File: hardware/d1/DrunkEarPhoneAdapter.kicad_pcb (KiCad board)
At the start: 2 copper layers, 40.3 x 34.7 mm, 9 parts, among them U1 CS43131-CNZR, U2 STM32G0B1VCT6, U4 TCPP03-M20, U5 TCPP03-M20, U6 ES8327, X1 X322516MLB4SI, X2 OT7EL89CJI-111YLC-24_576M

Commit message: New components
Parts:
- added R1: 10k, Resistor_SMD:R_0603_1608Metric, F.Cu at (28.3, 24.2)
- added U7: TPS7A2018PDBVR, JLCImport:TPS7A2018PDBVR, F.Cu at (30.1, 30.8)
- added U8: TPS7A2033PDBVR, JLCImport:TPS7A2033PDBVR, F.Cu at (24.9, 26.5)
- added U9: TPS560430XFDBVR, JLCImport:TPS560430XFDBVR, F.Cu at (25.2, 30.8)
- moved U6 17.5 mm to (44.3, 48.3)
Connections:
- U1 pad 38: unconnected-(U1-LRCK1-Pad38) -> /dac/I2S_WS
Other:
- copper layers 2 -> 4

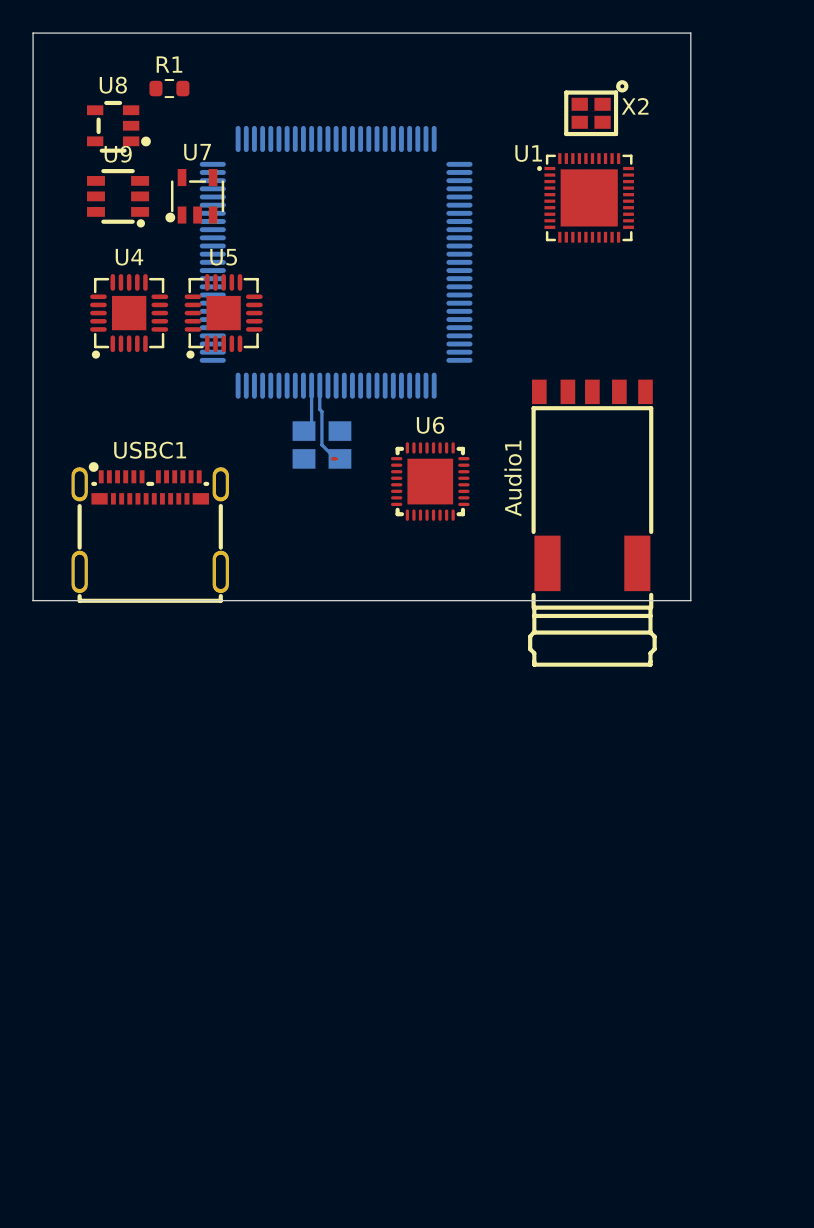
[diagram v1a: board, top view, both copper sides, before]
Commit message: Change uart pins, add components
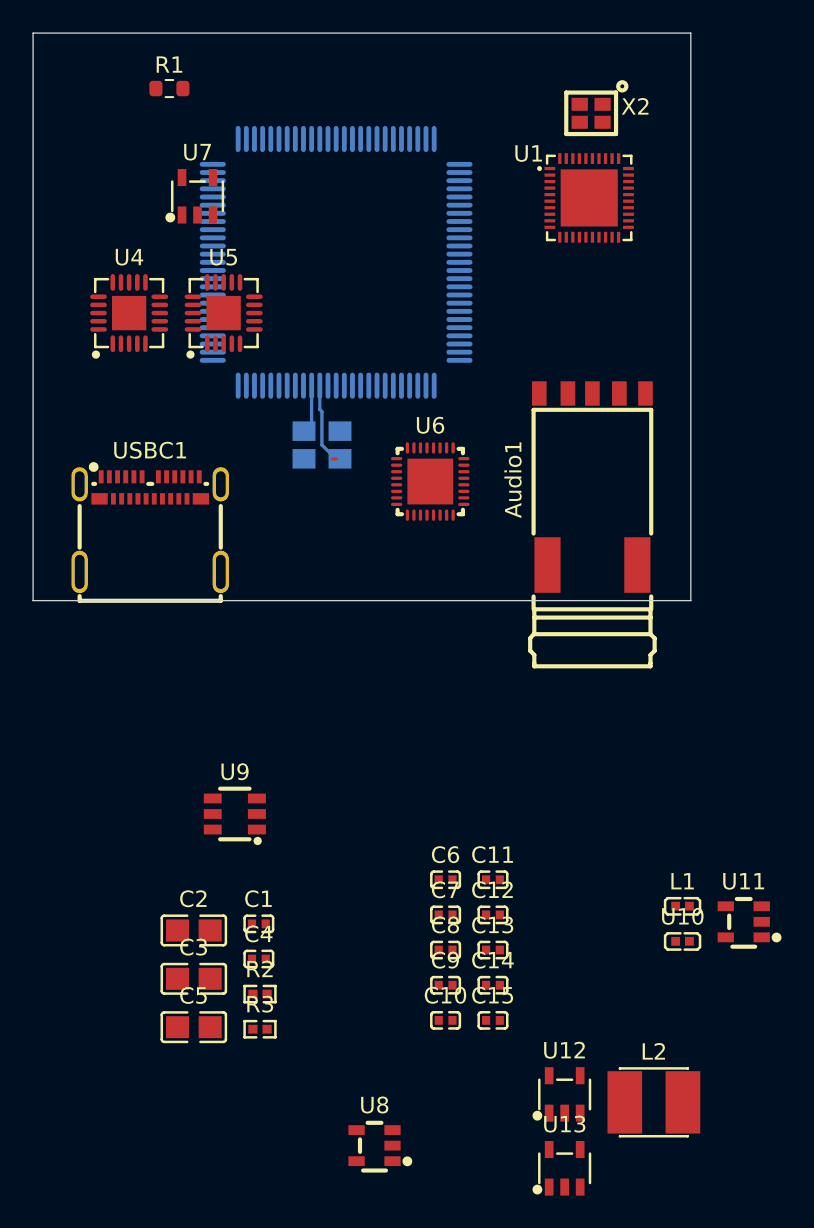
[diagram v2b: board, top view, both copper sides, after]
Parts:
- added C1: 100nF 16V X7R, JLCImport:CL05B104KO5NNNC, F.Cu at (33.8, 75.4)
- added C10: 1uF 25V X5R, JLCImport:CL05A105KA5NQNC, F.Cu at (45.2, 81.3)
- added C11: 1uF 25V X5R, JLCImport:CL05A105KA5NQNC, F.Cu at (48.1, 72.7)
- added C12: 1uF 25V X5R, JLCImport:CL05A105KA5NQNC, F.Cu at (48.1, 74.8)
- added C13: 4.7uF 10V X5R, JLCImport:CL05A475MP5NRNC, F.Cu at (48.1, 77.0)
- added C14: 1uF 25V X5R, JLCImport:CL05A105KA5NQNC, F.Cu at (48.1, 79.1)
- added C15: 1uF 25V X5R, JLCImport:CL05A105KA5NQNC, F.Cu at (48.1, 81.3)
- added C2: 2.2uF 50V X7R, JLCImport:CC0805KKX7R9BB225, F.Cu at (29.8, 75.8)
- added C3: 2.2uF 50V X7R, JLCImport:CC0805KKX7R9BB225, F.Cu at (29.8, 78.7)
- added C4: 100nF 50V X7R, JLCImport:CL05B104KB54PNC, F.Cu at (33.8, 77.5)
- added C5: 22uF 25V X5R, JLCImport:CL21A226MAQNNNE, F.Cu at (29.8, 81.7)
- added C6: 1uF 25V X5R, JLCImport:CL05A105KA5NQNC, F.Cu at (45.2, 72.7)
- added C7: 4.7uF 10V X5R, JLCImport:CL05A475MP5NRNC, F.Cu at (45.2, 74.8)
- added C8: 1uF 25V X5R, JLCImport:CL05A105KA5NQNC, F.Cu at (45.2, 77.0)
- added C9: 1uF 25V X5R, JLCImport:CL05A105KA5NQNC, F.Cu at (45.2, 79.1)
- added L1: BLM15AG601SN1D, JLCImport:BLM15AG601SN1D, F.Cu at (59.8, 74.3)
- added L2: SWPA4020S150MT, JLCImport:SWPA4020S150MT, F.Cu at (58.0, 86.3)
- added R2: 62kΩ, JLCImport:0402WGF6202TCE, F.Cu at (33.9, 79.7)
- added R3: 22kΩ, JLCImport:0402WGF2202TCE, F.Cu at (33.9, 81.8)
- added U10: BLM15PX601SN1D, JLCImport:BLM15PX601SN1D, F.Cu at (59.8, 76.4)
- added U11: TPS7A2033PDBVR, JLCImport:TPS7A2033PDBVR, F.Cu at (63.5, 75.3)
- added U12: TPS7A2018PDBVR, JLCImport:TPS7A2018PDBVR, F.Cu at (52.5, 85.8)
- added U13: TPS7A2018PDBVR, JLCImport:TPS7A2018PDBVR, F.Cu at (52.5, 90.3)
- moved U8 64.4 mm to (40.9, 89.0)
- moved U9 38.5 mm to (32.4, 68.7)
- moved Audio1 0.10 mm to (54.2, 48.2)
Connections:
- net /dac/JACK_RING_2 renamed /headset/JACK_RING_2
- Audio1 pad 1: /dac/JACK_SLEEVE -> /headset/JACK_SLEEVE
- Audio1 pad 2: /dac/JACK_TIP_DETECT -> /headset/JACK_TIP_DETECT
- Audio1 pad 3: /dac/JACK_RING_1 -> /headset/JACK_RING_1
- Audio1 pad 5: /dac/JACK_TIP -> /headset/JACK_TIP
- U7 pad 1: unconnected-(U7-IN-Pad1) -> +3V8
- U7 pad 2: unconnected-(U7-GND-Pad2) -> GND
- U7 pad 3: unconnected-(U7-EN-Pad3) -> +3V8
- U7 pad 5: unconnected-(U7-OUT-Pad5) -> +1V8_D
- U8 pad 3: unconnected-(U8-EN-Pad3) -> +1V8_D
- U8 pad 5: unconnected-(U8-OUT-Pad5) -> +3V3_D
- U9 pad 1: unconnected-(U9-CB-Pad1) -> Net-(U9-CB)
- U9 pad 2: unconnected-(U9-GND-Pad2) -> GND
- U9 pad 3: unconnected-(U9-FB-Pad3) -> Net-(U9-FB)
- U9 pad 4: unconnected-(U9-EN-Pad4) -> PWR_IN
- U9 pad 5: unconnected-(U9-VIN-Pad5) -> PWR_IN
- U9 pad 6: unconnected-(U9-SW-Pad6) -> Net-(U9-SW)

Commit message: Add new parts
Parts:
- removed R1: 10k, Resistor_SMD:R_0603_1608Metric
- added C16: 4.7uF 10V X5R, JLCImport:CL05A475MP5NRNC, F.Cu at (27.4, 104.2)
- added C17: 1uF 25V X5R, JLCImport:CL05A105KA5NQNC, F.Cu at (27.4, 106.3)
- added C18: 1uF 25V X5R, JLCImport:CL05A105KA5NQNC, F.Cu at (35.6, 104.2)
- added C19: 100nF 16V X7R, JLCImport:CL05B104KO5NNNC, F.Cu at (27.4, 108.5)
- added C20: 100nF 16V X7R, JLCImport:CL05B104KO5NNNC, F.Cu at (35.6, 106.3)
- added C21: 100nF 16V X7R, JLCImport:CL05B104KO5NNNC, F.Cu at (27.4, 110.6)
- added C22: 100nF 16V X7R, JLCImport:CL05B104KO5NNNC, F.Cu at (27.4, 112.8)
- added C23: 100nF 16V X7R, JLCImport:CL05B104KO5NNNC, F.Cu at (27.4, 114.9)
- added C24: 100nF 16V X7R, JLCImport:CL05B104KO5NNNC, F.Cu at (55.2, 101.9)
- added C25: 2.2uF 16V X5R, JLCImport:CL05A225KO5NQNC, F.Cu at (55.2, 104.0)
- added C26: 15uF 35V X5R, JLCImport:C2012X5R1V156MT000E, F.Cu at (59.2, 102.3)
- added C27: 15uF 35V X5R, JLCImport:C2012X5R1V156MT000E, F.Cu at (59.2, 105.2)
- added C28: 2.2uF 16V X5R, JLCImport:CL05A225KO5NQNC, F.Cu at (55.2, 106.2)
- added C29: 2.2uF 16V X5R, JLCImport:CL05A225KO5NQNC, F.Cu at (51.4, 117.7)
- added C30: 2.2uF 16V X5R, JLCImport:CL05A225KO5NQNC, F.Cu at (51.4, 119.8)
- added C31: 2.2uF 16V X5R, JLCImport:CL05A225KO5NQNC, F.Cu at (51.4, 122.0)
- added C32: 2.2uF 16V X5R, JLCImport:CL05A225KO5NQNC, F.Cu at (51.4, 124.1)
- added C33: 2.2uF 16V X5R, JLCImport:CL05A225KO5NQNC, F.Cu at (51.4, 126.3)
- added C34: 2.2uF 16V X5R, JLCImport:CL05A225KO5NQNC, F.Cu at (51.4, 128.4)
- added L3: BLM15AG601SN1D, JLCImport:BLM15AG601SN1D, F.Cu at (30.5, 106.3)
- added L4: BLM15AG601SN1D, JLCImport:BLM15AG601SN1D, F.Cu at (38.7, 104.2)
- added U14: BLM15PX601SN1D, JLCImport:BLM15PX601SN1D, F.Cu at (30.5, 108.5)
- moved L1 37.0 mm to (30.4, 96.9)
- moved X2 0.60 mm to (53.9, 26.3)
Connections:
- net /dac/JACK_SLEEVE renamed /dac/JACK_DETECTED_GND
- C12 pad 2: +3V8 -> Net-(U12-EN)
- L1 pad 1: unconnected-(L1-Pad1) -> +1V8_D
- L1 pad 2: unconnected-(L1-Pad2) -> Net-(X2-VDD)
- U1 pad 10: unconnected-(U1-FLYP_VA-Pad10) -> /dac/FLYP_VA
- U1 pad 11: unconnected-(U1-FLYN_VA-Pad11) -> /dac/FLYN_VA
- U1 pad 18: unconnected-(U1-VCP_FILT–-Pad18) -> /dac/VCP_FILT-
- U1 pad 19: unconnected-(U1-GNDCP-Pad19) -> /dac/GNDCP
- U1 pad 20: unconnected-(U1-FLYN_VCP-Pad20) -> /dac/FLYN_VCP
- U1 pad 21: unconnected-(U1-VCP_FILT+-Pad21) -> /dac/VCP_FILT+
- U1 pad 23: unconnected-(U1-FLYC_VCP-Pad23) -> /dac/FLYC_VCP
- U1 pad 24: unconnected-(U1-FLYP_VCP-Pad24) -> /dac/FLYP_VCP
- U1 pad 25: unconnected-(U1-VCP-Pad25) -> /dac/VCP
- U1 pad 26: unconnected-(U1-VP-Pad26) -> Net-(U1-VP)
- U1 pad 28: unconnected-(U1-RESET#-Pad28) -> /dac/DAC_RESET
- U1 pad 31: unconnected-(U1-VL-Pad31) -> Net-(U1-VD)
- U1 pad 35: unconnected-(U1-GNDD-Pad35) -> GND
- U1 pad 4: unconnected-(U1-VD-Pad4) -> Net-(U1-VD)
- U1 pad 41: unconnected-(U1-EP-Pad41) -> GND
- U1 pad 5: unconnected-(U1-FILT+-Pad5) -> /dac/FILT+
- U1 pad 6: unconnected-(U1-FILT–-Pad6) -> /dac/FILT-
- U1 pad 7: unconnected-(U1-VA-Pad7) -> +1V8_A
- U1 pad 8: unconnected-(U1-GNDA-Pad8) -> GND
- U1 pad 9: unconnected-(U1--VA-Pad9) -> /dac/-VA
- U10 pad 1: unconnected-(U10-Pad1) -> +3V8
- U10 pad 2: unconnected-(U10-Pad2) -> Net-(U12-EN)
- U12 pad 1: +3V8 -> Net-(U12-EN)
- U12 pad 3: +3V8 -> Net-(U12-EN)
- U2 pad 12: unconnected-(U2-VREF+-Pad12) -> Net-(U2-VREF+)
- U2 pad 14: unconnected-(U2-VSS/VSSA-Pad14) -> GND
- U2 pad 19: /mcu/UART_TX -> unconnected-(U2-PF4-Pad19)
- U2 pad 20: /mcu/UART_RX -> unconnected-(U2-PF5-Pad20)
- U2 pad 57: unconnected-(U2-PC6-Pad57) -> /mcu/UART_TX
- U2 pad 58: unconnected-(U2-PC7-Pad58) -> /mcu/UART_RX
- U2 pad 63: unconnected-(U2-VSS-Pad63) -> GND
- X1 pad 2: GND -> Net-(X1-GND-Pad2)
- X1 pad 4: GND -> Net-(X1-GND-Pad2)
- X2 pad 2: unconnected-(X2-GND-Pad2) -> GND
- X2 pad 4: unconnected-(X2-VDD-Pad4) -> Net-(X2-VDD)
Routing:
- net Net-(U1-XTI/MCLK): track 0.00 -> 1.78 mm

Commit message: Pre-finalize sch
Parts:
- removed X2: OT7EL89CJI-111YLC-24_576M, JLCImport:OT7EL89CJI-111YLC-24_576M
- added C35: 100nF 16V X7R, JLCImport:CL05B104KO5NNNC, F.Cu at (78.8, 71.6)
- added C36: 1uF 25V X5R, JLCImport:CL05A105KA5NQNC, F.Cu at (78.8, 73.7)
- added C37: 100nF 16V X7R, JLCImport:CL05B104KO5NNNC, F.Cu at (78.8, 75.9)
- added C38: 1uF 25V X5R, JLCImport:CL05A105KA5NQNC, F.Cu at (81.7, 71.6)
- added C39: 100nF 16V X7R, JLCImport:CL05B104KO5NNNC, F.Cu at (81.7, 73.7)
- added C40: 100nF 16V X7R, JLCImport:CL05B104KO5NNNC, F.Cu at (81.7, 75.9)
- added C41: 1uF 25V X5R, JLCImport:CL05A105KA5NQNC, F.Cu at (84.6, 71.6)
- added C42: 1uF 25V X5R, JLCImport:CL05A105KA5NQNC, F.Cu at (84.6, 73.7)
- added C43: 1uF 25V X5R, JLCImport:CL05A105KA5NQNC, F.Cu at (84.6, 75.9)
- added C44: 100nF 16V X7R, JLCImport:CL05B104KO5NNNC, F.Cu at (96.6, 61.8)
- added C45: 1uF 25V X5R, JLCImport:CL05A105KA5NQNC, F.Cu at (88.8, 51.9)
- added C46: 1uF 25V X5R, JLCImport:CL05A105KA5NQNC, F.Cu at (88.8, 54.0)
- added C47: 1uF 25V X5R, JLCImport:CL05A105KA5NQNC, F.Cu at (88.8, 56.2)
- added C48: 1uF 25V X5R, JLCImport:CL05A105KA5NQNC, F.Cu at (88.8, 58.3)
- added C49: 10nF 50V X7R, Capacitor_SMD:C_0402_1005Metric, F.Cu at (41.4, 125.2)
- added C50: 100nF 16V X7R, JLCImport:CL05B104KO5NNNC, F.Cu at (38.5, 121.0)
- added C51: 22uF 25V X5R, JLCImport:CL21A226MAQNNNE, F.Cu at (86.4, 30.9)
- added C52: 100nF 16V X7R, JLCImport:CL05B104KO5NNNC, F.Cu at (38.5, 123.1)
- added C53: 4.7uF 10V X5R, JLCImport:CL05A475MP5NRNC, F.Cu at (38.5, 125.3)
- added C54: 100nF 16V X7R, JLCImport:CL05B104KO5NNNC, F.Cu at (38.5, 127.4)
- added C55: 4.7uF 10V X5R, JLCImport:CL05A475MP5NRNC, F.Cu at (38.5, 129.6)
- added C56: 100nF 16V X7R, JLCImport:CL05B104KO5NNNC, F.Cu at (96.8, 43.9)
- added C57: 22uF 25V X5R, JLCImport:CL21A226MAQNNNE, F.Cu at (86.4, 33.8)
- added C58: 22uF 25V X5R, JLCImport:CL21A226MAQNNNE, F.Cu at (86.4, 36.8)
- added C59: 22uF 25V X5R, JLCImport:CL21A226MAQNNNE, F.Cu at (86.4, 39.8)
- added C60: 22uF 25V X5R, JLCImport:CL21A226MAQNNNE, F.Cu at (86.4, 42.7)
- added C61: 22uF 25V X5R, JLCImport:CL21A226MAQNNNE, F.Cu at (86.4, 45.7)
- added C62: 22uF 25V X5R, JLCImport:CL21A226MAQNNNE, F.Cu at (86.4, 48.6)
- added C63: 22uF 25V X5R, JLCImport:CL21A226MAQNNNE, F.Cu at (86.4, 51.6)
- added C64: 22uF 25V X5R, JLCImport:CL21A226MAQNNNE, F.Cu at (86.4, 54.6)
- added C65: 22uF 25V X5R, JLCImport:CL21A226MAQNNNE, F.Cu at (86.4, 57.5)
- added C66: 10nF 50V X7R, Capacitor_SMD:C_0402_1005Metric, F.Cu at (8.91, 17.3)
- added C67: 2.2uF 50V X7R, JLCImport:CC0805KKX7R9BB225, F.Cu at (4.95, 15.6)
- added C68: 2.2uF 50V X7R, JLCImport:CC0805KKX7R9BB225, F.Cu at (4.95, 18.6)
- added C69: 100nF 50V X7R, JLCImport:CL05B104KB54PNC, F.Cu at (8.93, 15.2)
- added C70: 330pF 50V, Capacitor_SMD:C_0402_1005Metric, F.Cu at (93.1, 88.3)
- added C71: 330pF 50V, Capacitor_SMD:C_0402_1005Metric, F.Cu at (93.1, 90.3)
- added C72: 330pF 50V, Capacitor_SMD:C_0402_1005Metric, F.Cu at (93.1, 92.2)
- added C73: 330pF 50V, Capacitor_SMD:C_0402_1005Metric, F.Cu at (93.1, 94.2)
- added C74: 100nF 16V X7R, JLCImport:CL05B104KO5NNNC, F.Cu at (78.6, 102.4)
- added C75: 100nF 50V X7R, JLCImport:CL05B104KB54PNC, F.Cu at (78.6, 104.5)
- added C76: 1uF 25V X5R, JLCImport:CL05A105KA5NQNC, F.Cu at (83.4, 106.7)
- added C77: 100nF 16V X7R, JLCImport:CL05B104KO5NNNC, F.Cu at (83.4, 108.8)
- added C78: 100nF 16V X7R, JLCImport:CL05B104KO5NNNC, F.Cu at (83.4, 111.0)
- added C79: 100nF 16V X7R, JLCImport:CL05B104KO5NNNC, F.Cu at (83.4, 113.1)
- added D1: PMEG4010CEH_115, Diode_SMD:D_SOD-110, F.Cu at (97.5, 36.3)
- added D2: B5819WS_C916992, Diode_SMD:D_SOD-323, F.Cu at (91.1, 33.8)
- added D3: PMEG4010CEH_115, Diode_SMD:D_SOD-110, F.Cu at (97.5, 39.3)
- added L5: BLM15AG601SN1D, JLCImport:BLM15AG601SN1D, F.Cu at (79.0, 78.0)
- added L6: BLM15AG601SN1D, JLCImport:BLM15AG601SN1D, F.Cu at (79.0, 80.2)
- added L7: ECMF02-2AMX6, JLCImport:ECMF02-2AMX6, F.Cu at (103.5, 88.2)
- added Q1: CSD17577Q3A, JLCImport:CSD17577Q3A, F.Cu at (24.1, 30.5)
- added Q2: CSD17577Q3A, JLCImport:CSD17577Q3A, F.Cu at (24.0, 23.9)
- added R1: 33Ω, Resistor_SMD:R_0402_1005Metric, F.Cu at (96.1, 102.3)
- added R10: 10kΩ, Resistor_SMD:R_0402_1005Metric, F.Cu at (91.7, 51.8)
- added R11: 2.2kΩ, Resistor_SMD:R_0402_1005Metric, F.Cu at (96.7, 51.8)
- added R12: 2.2kΩ, Resistor_SMD:R_0402_1005Metric, F.Cu at (96.7, 53.8)
- added R13: 10kΩ, Resistor_SMD:R_0402_1005Metric, F.Cu at (91.7, 53.8)
- added R14: 100kΩ, JLCImport:0402WGF1003TCE, F.Cu at (41.5, 121.0)
- added R15: 100kΩ, JLCImport:0402WGF1003TCE, F.Cu at (41.5, 123.1)
- added R16: 33Ω 0805, Resistor_SMD:R_0805_2012Metric, F.Cu at (91.2, 30.9)
- added R17: 10mΩ 500mW, Resistor_SMD:R_0805_2012Metric, F.Cu at (101.9, 36.2)
- added R18: 10mΩ 500mW, Resistor_SMD:R_0805_2012Metric, F.Cu at (101.9, 39.2)
- added R19: 10kΩ, Resistor_SMD:R_0402_1005Metric, F.Cu at (0.95, 15.1)
- added R20: 560Ω, Resistor_SMD:R_0402_1005Metric, F.Cu at (0.95, 17.1)
- added R21: 130kΩ, Resistor_SMD:R_0402_1005Metric, F.Cu at (0.95, 19.1)
- added R22: 10kΩ, Resistor_SMD:R_0402_1005Metric, F.Cu at (0.95, 21.1)
- added R23: 0Ω, Resistor_SMD:R_0402_1005Metric, F.Cu at (75.7, 102.3)
- added R24: 47kΩ, Resistor_SMD:R_0402_1005Metric, F.Cu at (75.7, 104.3)
- added R25: 47kΩ, Resistor_SMD:R_0402_1005Metric, F.Cu at (75.7, 106.3)
- added R26: 10kΩ, Resistor_SMD:R_0402_1005Metric, F.Cu at (75.7, 108.3)
- added R27: 560Ω, Resistor_SMD:R_0402_1005Metric, F.Cu at (75.7, 110.3)
- added R28: 130kΩ, Resistor_SMD:R_0402_1005Metric, F.Cu at (75.7, 112.2)
- added R29: 10kΩ, Resistor_SMD:R_0402_1005Metric, F.Cu at (75.7, 114.2)
- added R30: 0Ω, Resistor_SMD:R_0402_1005Metric, F.Cu at (75.7, 116.2)
- added R4: 100kΩ, JLCImport:0402WGF1003TCE, F.Cu at (89.6, 71.6)
- added R5: 10kΩ, Resistor_SMD:R_0402_1005Metric, F.Cu at (96.1, 104.3)
- added R6: 100kΩ, JLCImport:0402WGF1003TCE, F.Cu at (89.6, 75.9)
- added R7: 33Ω, Resistor_SMD:R_0402_1005Metric, F.Cu at (96.1, 106.3)
- added R8: 10kΩ, Resistor_SMD:R_0402_1005Metric, F.Cu at (96.1, 108.3)
- added R9: 33Ω, Resistor_SMD:R_0402_1005Metric, F.Cu at (96.7, 57.8)
- added SW1: SSSS811101, JLCImport:SSSS811101, F.Cu at (45.2, 53.6)
- added U15: ESDA25P35-1U1M, JLCImport:ESDA25P35-1U1M_C19829649, F.Cu at (105.8, 30.7)
- added U16: ESDA25P35-1U1M, JLCImport:ESDA25P35-1U1M_C19829649, F.Cu at (105.8, 33.3)
- added U18: TPS22917DBVR, JLCImport:TPS22917DBVR, F.Cu at (87.3, 103.5)
- added U19: TPS22917DBVR, JLCImport:TPS22917DBVR, F.Cu at (87.3, 108.1)
- added USBC2: ~, JLCImport:USBC_EXT_5P, F.Cu at (34.1, 24.0)
- added X3: 24.576MHz, JLCImport:SX2M22_5792M20F30TNN, F.Cu at (92.3, 107.8)
- X1: value X322516MLB4SI -> 22.5792MHz; footprint JLCImport:X322516MLB4SI -> JLCImport:SX2M22_5792M20F30TNN; moved to F.Cu
- moved X1 79.2 mm to (92.3, 103.4)
- moved C17 56.1 mm to (83.4, 102.4)
- moved C19 56.1 mm to (83.4, 104.5)
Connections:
- Audio1 pad 1: /headset/JACK_SLEEVE -> /adc/GMS1
- Audio1 pad 2: /headset/JACK_TIP_DETECT -> /dac/JACK_TIP_DETECT
- Audio1 pad 3: /headset/JACK_RING_1 -> /dac/JACK_RING_1
- Audio1 pad 4: /headset/JACK_RING_2 -> +3V3_D
- Audio1 pad 5: /headset/JACK_TIP -> /dac/JACK_TIP
- Audio1 pad 6: unconnected-(Audio1-Pad6) -> +3V3_D
- Audio1 pad 7: unconnected-(Audio1-Pad7) -> +3V3_D
- C10 pad 1: GND -> +3V3_D
- C11 pad 1: GND -> +3V3_D
- C12 pad 1: GND -> +3V3_D
- C13 pad 1: GND -> +3V3_D
- C14 pad 1: GND -> +3V3_D
- C15 pad 1: GND -> +3V3_D
- C16 pad 2: GND -> +3V3_D
- C17 pad 1: GND -> +3V3_D
- C17 pad 2: Net-(X2-VDD) -> Net-(U18-QOD)
- C18 pad 2: GND -> +3V3_D
- C19 pad 1: Net-(X2-VDD) -> Net-(U18-QOD)
- C19 pad 2: GND -> +3V3_D
- C2 pad 2: GND -> +3V3_D
- C20 pad 2: GND -> +3V3_D
- C21 pad 1: GND -> +3V3_D
- C22 pad 2: GND -> +3V3_D
- C23 pad 1: GND -> +3V3_D
- C24 pad 2: GND -> +3V3_D
- C25 pad 2: GND -> +3V3_D
- C28 pad 2: GND -> +3V3_D
- C3 pad 2: GND -> +3V3_D
- C30 pad 1: /dac/VCP -> +1V8_CP
- C30 pad 2: GND -> +3V3_D
- C31 pad 2: /dac/GNDCP -> +3V3_D
- C32 pad 1: /dac/GNDCP -> +3V3_D
- C4 pad 2: GND -> +3V3_D
- C5 pad 2: GND -> +3V3_D
- C6 pad 1: GND -> +3V3_D
- C7 pad 1: GND -> +3V3_D
- C8 pad 1: GND -> +3V3_D
- C9 pad 1: GND -> +3V3_D
- L1 pad 2: Net-(X2-VDD) -> Net-(U18-VIN)
- R3 pad 2: GND -> +3V3_D
- U1 pad 1: /dac/I2C_SCL -> /adc/I2C_SCL
- U1 pad 13: /dac/JACK_DETECTED_GND -> +3V3_D
- U1 pad 17: /dac/JACK_DETECTED_GND -> +3V3_D
- U1 pad 19: /dac/GNDCP -> +3V3_D
- U1 pad 25: /dac/VCP -> +1V8_CP
- U1 pad 27: unconnected-(U1-INT#-Pad27) -> /dac//INT
- U1 pad 30: unconnected-(U1-ADR-Pad30) -> +3V3_D
- U1 pad 33: unconnected-(U1-CLKOUT-Pad33) -> Net-(U1-CLKOUT)
- U1 pad 35: GND -> +3V3_D
- U1 pad 36: unconnected-(U1-XTO-Pad36) -> +3V3_D
- U1 pad 39: /dac/I2C_SDA -> /adc/I2C_SDA
- U1 pad 41: GND -> +3V3_D
- U1 pad 8: GND -> +3V3_D
- U11 pad 2: GND -> +3V3_D
- U12 pad 2: GND -> +3V3_D
- U13 pad 2: GND -> +3V3_D
- U2 pad 1: /mcu/I2S2_WS -> /adc/I2S_WS
- U2 pad 11: unconnected-(U2-VBAT-Pad11) -> +1V8_D
- U2 pad 13: unconnected-(U2-VDD/VDDA-Pad13) -> +1V8_D
- U2 pad 14: GND -> +3V3_D
- U2 pad 15: Net-(U2-PF0-OSC_IN) -> unconnected-(U2-PF0-OSC_IN-Pad15)
- U2 pad 16: Net-(U2-PF1-OSC_OUT) -> unconnected-(U2-PF1-OSC_OUT-Pad16)
- U2 pad 17: unconnected-(U2-PF2-NRST-Pad17) -> Net-(U2-PF2-NRST)
- U2 pad 24: /mcu/I2S2_SD -> /adc/I2S_SD
- U2 pad 25: unconnected-(U2-PA0-Pad25) -> /mcu/ADC1_IN1
- U2 pad 26: unconnected-(U2-PA1-Pad26) -> /mcu/ADC1_IN2
- U2 pad 27: unconnected-(U2-PA2-Pad27) -> /mcu/ADC1_IN3
- U2 pad 28: unconnected-(U2-PA3-Pad28) -> /mcu/ADC1_IN4
- U2 pad 29: unconnected-(U2-PA4-Pad29) -> /mcu/ADC1_IN5
- U2 pad 30: /mcu/I2S1_CK -> /dac/I2S_CK
- U2 pad 32: /mcu/I2S1_SD -> /dac/I2S_SD
- U2 pad 35: /mcu/I2S1_WS -> /dac/I2S_WS
- U2 pad 49: /mcu/I2S2_CK -> /adc/I2S_CK
- U2 pad 56: /mcu/I2C2_SCL -> unconnected-(U2-PA9-Pad56)
- U2 pad 63: GND -> +3V3_D
- U2 pad 64: unconnected-(U2-VDDIO2-Pad64) -> +3V3_D
- U2 pad 69: /mcu/I2C2_SDA -> unconnected-(U2-PA10-Pad69)
- U2 pad 98: unconnected-(U2-PB6-Pad98) -> /mcu/I2C2_SCL
- U2 pad 99: unconnected-(U2-PB7-Pad99) -> /mcu/I2C2_SDA
- U4 pad 1: unconnected-(U4-CC1-Pad1) -> /mcu/UCPD1_CC1
- U4 pad 10: unconnected-(U4-Isense-Pad10) -> /ucpd/USB_PHONE_ISENSE
- U4 pad 11: unconnected-(U4-Vsense-Pad11) -> /ucpd/VSENSE_PHONE
- U4 pad 12: unconnected-(U4-GND-Pad12) -> +3V3_D
- U4 pad 13: unconnected-(U4-CC2c-Pad13) -> /ucpd/USB_PHONE_CC2
- U4 pad 14: unconnected-(U4-CBIAS-Pad14) -> Net-(U4-CBIAS)
- U4 pad 15: unconnected-(U4-CC1c-Pad15) -> /ucpd/USB_PHONE_CC1
- U4 pad 16: unconnected-(U4-I2C_ADD-Pad16) -> +3V3_D
- U4 pad 17: unconnected-(U4-SDA-Pad17) -> /adc/I2C_SDA
- U4 pad 18: unconnected-(U4-SCL-Pad18) -> /adc/I2C_SCL
- U4 pad 19: unconnected-(U4-FLGn-Pad19) -> /mcu/GPIO_EXTI3
- U4 pad 2: unconnected-(U4-VCC_VCONN-Pad2) -> +3V3_D
- U4 pad 20: unconnected-(U4-EN-Pad20) -> +1V8_D
- U4 pad 21: unconnected-(U4-GND-Pad21) -> +3V3_D
- U4 pad 3: unconnected-(U4-CC2-Pad3) -> /mcu/UCPD1_CC2
- U4 pad 4: unconnected-(U4-IANA-Pad4) -> Net-(U4-IANA)
- U4 pad 5: unconnected-(U4-GDPg-Pad5) -> /ucpd/GDPg
- U4 pad 6: unconnected-(U4-GDPs-Pad6) -> /ucpd/GDPs
- U4 pad 9: unconnected-(U4-VBUSc-Pad9) -> /ucpd/USB_PHONE_VBUS
- U5 pad 1: unconnected-(U5-CC1-Pad1) -> /mcu/UCPD2_CC1
- U5 pad 10: unconnected-(U5-Isense-Pad10) -> /ucpd/USB_CHR_ISENSE
- U5 pad 11: unconnected-(U5-Vsense-Pad11) -> /ucpd/VSENSE_CHR
- U5 pad 12: unconnected-(U5-GND-Pad12) -> +3V3_D
- U5 pad 13: unconnected-(U5-CC2c-Pad13) -> /ucpd/USB_CHR_CC2
- U5 pad 14: unconnected-(U5-CBIAS-Pad14) -> Net-(U5-CBIAS)
- U5 pad 15: unconnected-(U5-CC1c-Pad15) -> /ucpd/USB_CHR_CC1
- U5 pad 16: unconnected-(U5-I2C_ADD-Pad16) -> +1V8_D
- U5 pad 17: unconnected-(U5-SDA-Pad17) -> /adc/I2C_SDA
- U5 pad 18: unconnected-(U5-SCL-Pad18) -> /adc/I2C_SCL
- U5 pad 19: unconnected-(U5-FLGn-Pad19) -> /mcu/GPIO_EXTI4
- U5 pad 2: unconnected-(U5-VCC_VCONN-Pad2) -> +3V3_D
- U5 pad 20: unconnected-(U5-EN-Pad20) -> +1V8_D
- U5 pad 21: unconnected-(U5-GND-Pad21) -> +3V3_D
- U5 pad 3: unconnected-(U5-CC2-Pad3) -> /mcu/UCPD2_CC2
- U5 pad 4: unconnected-(U5-IANA-Pad4) -> Net-(U5-IANA)
- U5 pad 9: unconnected-(U5-VBUSc-Pad9) -> /ucpd/USB_CHR_VBUS
- U6 pad 1: unconnected-(U6-MCLK/DMIC_SDA-Pad1) -> /adc/CLKIN
- U6 pad 10: unconnected-(U6-INTOUT-Pad10) -> /adc/INT/
- U6 pad 11: unconnected-(U6-CPVDD-Pad11) -> Net-(U6-CPVDD)
- U6 pad 12: unconnected-(U6-CPTOP-Pad12) -> /adc/CPTOP
- U6 pad 13: unconnected-(U6-GMS0-Pad13) -> +3V3_D
- U6 pad 14: unconnected-(U6-CPGND-Pad14) -> +3V3_D
- U6 pad 15: unconnected-(U6-GMS1-Pad15) -> /adc/GMS1
- U6 pad 16: unconnected-(U6-CPBOT-Pad16) -> /adc/CPBOT
- U6 pad 17: unconnected-(U6-CPVSSP-Pad17) -> Net-(U6-CPVSSP)
- U6 pad 2: unconnected-(U6-DVDD-Pad2) -> +3V3_D
- U6 pad 20: unconnected-(U6-DACVREF-Pad20) -> Net-(U6-DACVREF)
- U6 pad 21: unconnected-(U6-AVDD-Pad21) -> Net-(U6-AVDD)
- U6 pad 22: unconnected-(U6-AGND-Pad22) -> +3V3_D
- U6 pad 23: unconnected-(U6-ADCVREF-Pad23) -> Net-(U6-ADCVREF)
- U6 pad 24: unconnected-(U6-VMID-Pad24) -> Net-(U6-VMID)
- U6 pad 25: unconnected-(U6-MIC1N-Pad25) -> /adc/MIC1N
- U6 pad 26: unconnected-(U6-MIC1P-Pad26) -> /adc/MIC1P
- U6 pad 3: unconnected-(U6-PVDD-Pad3) -> +1V8_D
- U6 pad 30: unconnected-(U6-CE-Pad30) -> +3V3_D
- U6 pad 31: unconnected-(U6-CDATA-Pad31) -> /adc/I2C_SDA
- U6 pad 32: unconnected-(U6-CCLK-Pad32) -> /adc/I2C_SCL
- U6 pad 33: unconnected-(U6-EP-Pad33) -> +3V3_D
- U6 pad 4: unconnected-(U6-DGND-Pad4) -> +3V3_D
- U6 pad 5: unconnected-(U6-SCLK-Pad5) -> /adc/I2S_CK
- U6 pad 6: unconnected-(U6-SDIN-Pad6) -> +3V3_D
- U6 pad 7: unconnected-(U6-LRCK-Pad7) -> /adc/I2S_WS
- U6 pad 8: unconnected-(U6-SDOUT-Pad8) -> /adc/I2S_SD
- U6 pad 9: unconnected-(U6-HEADSET-Pad9) -> /adc/HEADSET
- U7 pad 2: GND -> +3V3_D
- U8 pad 2: GND -> +3V3_D
- U9 pad 2: GND -> +3V3_D
- USBC1 pad 0: Net-(USBC1-25) -> +3V3_D
- USBC1 pad A1: Net-(USBC1-GND-PadA1) -> +3V3_D
- USBC1 pad A12: Net-(USBC1-GND-PadA12) -> +3V3_D
- USBC1 pad B1: Net-(USBC1-GND-PadA12) -> +3V3_D
- USBC1 pad B12: Net-(USBC1-GND-PadA1) -> +3V3_D
- X1 pad 1: Net-(U2-PF1-OSC_OUT) -> Net-(U19-QOD)
- X1 pad 2: Net-(X1-GND-Pad2) -> +3V3_D
- X1 pad 3: Net-(U2-PF0-OSC_IN) -> Net-(X1-OUT)
- X1 pad 4: Net-(X1-GND-Pad2) -> Net-(U19-QOD)
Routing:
- net Net-(U2-PF0-OSC_IN): track 5.14 -> 0.00 mm
- net Net-(U2-PF1-OSC_OUT): track 2.97 -> 0.00 mm
- net Net-(U1-XTI/MCLK): track 1.78 -> 0.00 mm
